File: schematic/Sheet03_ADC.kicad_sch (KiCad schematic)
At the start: 15 parts, among them U1 ADC12DJ5200-SP

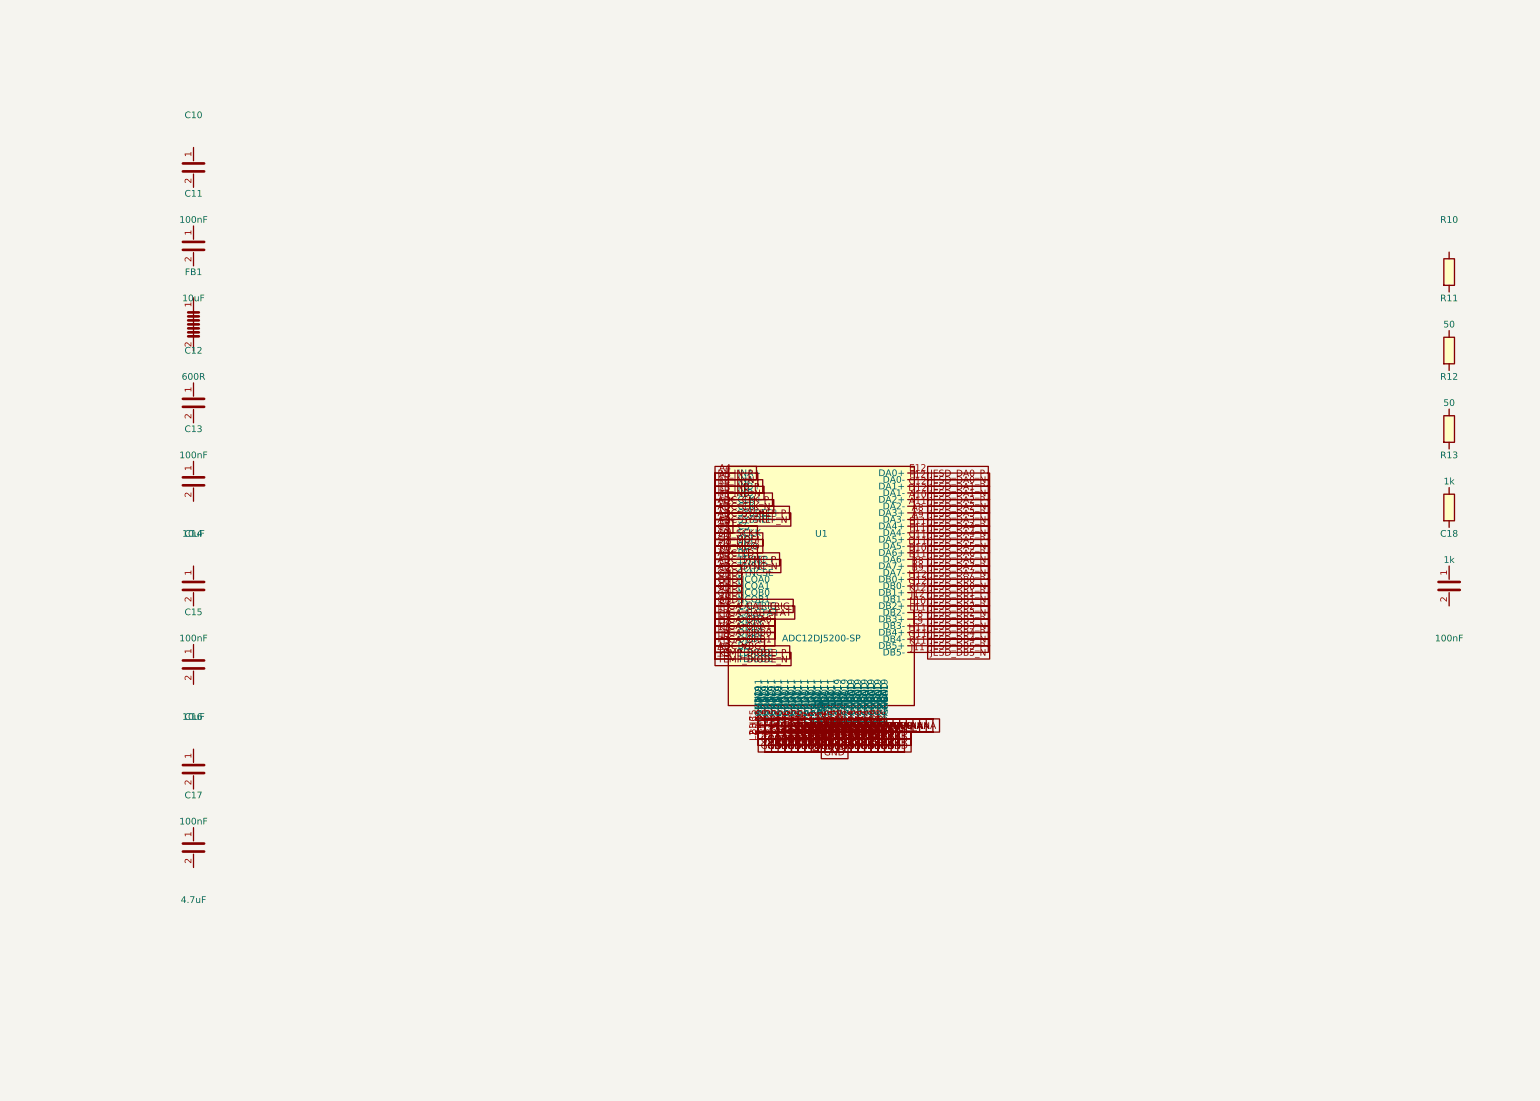
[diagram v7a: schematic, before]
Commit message: feat: connect ALL passive components and fix clock routing
- Added PASSIVE_TOPOLOGY dict mapping 139 passives to their nets
- Passive pin endpoints now get global_labels (was 0 connected, now 138)
- R38 intentionally GND-GND (RECAL_EN pull-down)
- Fixed LMK clock output mapping: CLKout0→ADC_CLK_P, CLKout2→FPGA_REFCLK_P, etc.
- Fixed TPS7H5001-SP SYNC pin collision with LMX_SYNC
- Total connections: 867 pins (up from 641)
- Cross-sheet nets: 52
- Power rails: VIN(33), +3V3(98), GND(228) all with decoupling
- JESD204C: U1↔U2 on 4 lanes ✓
- SPI: U1↔U2↔U3↔U4 ✓
- Clock: LMK→ADC (CLK+SYSREF), LMK→FPGA (REF+SPW) ✓
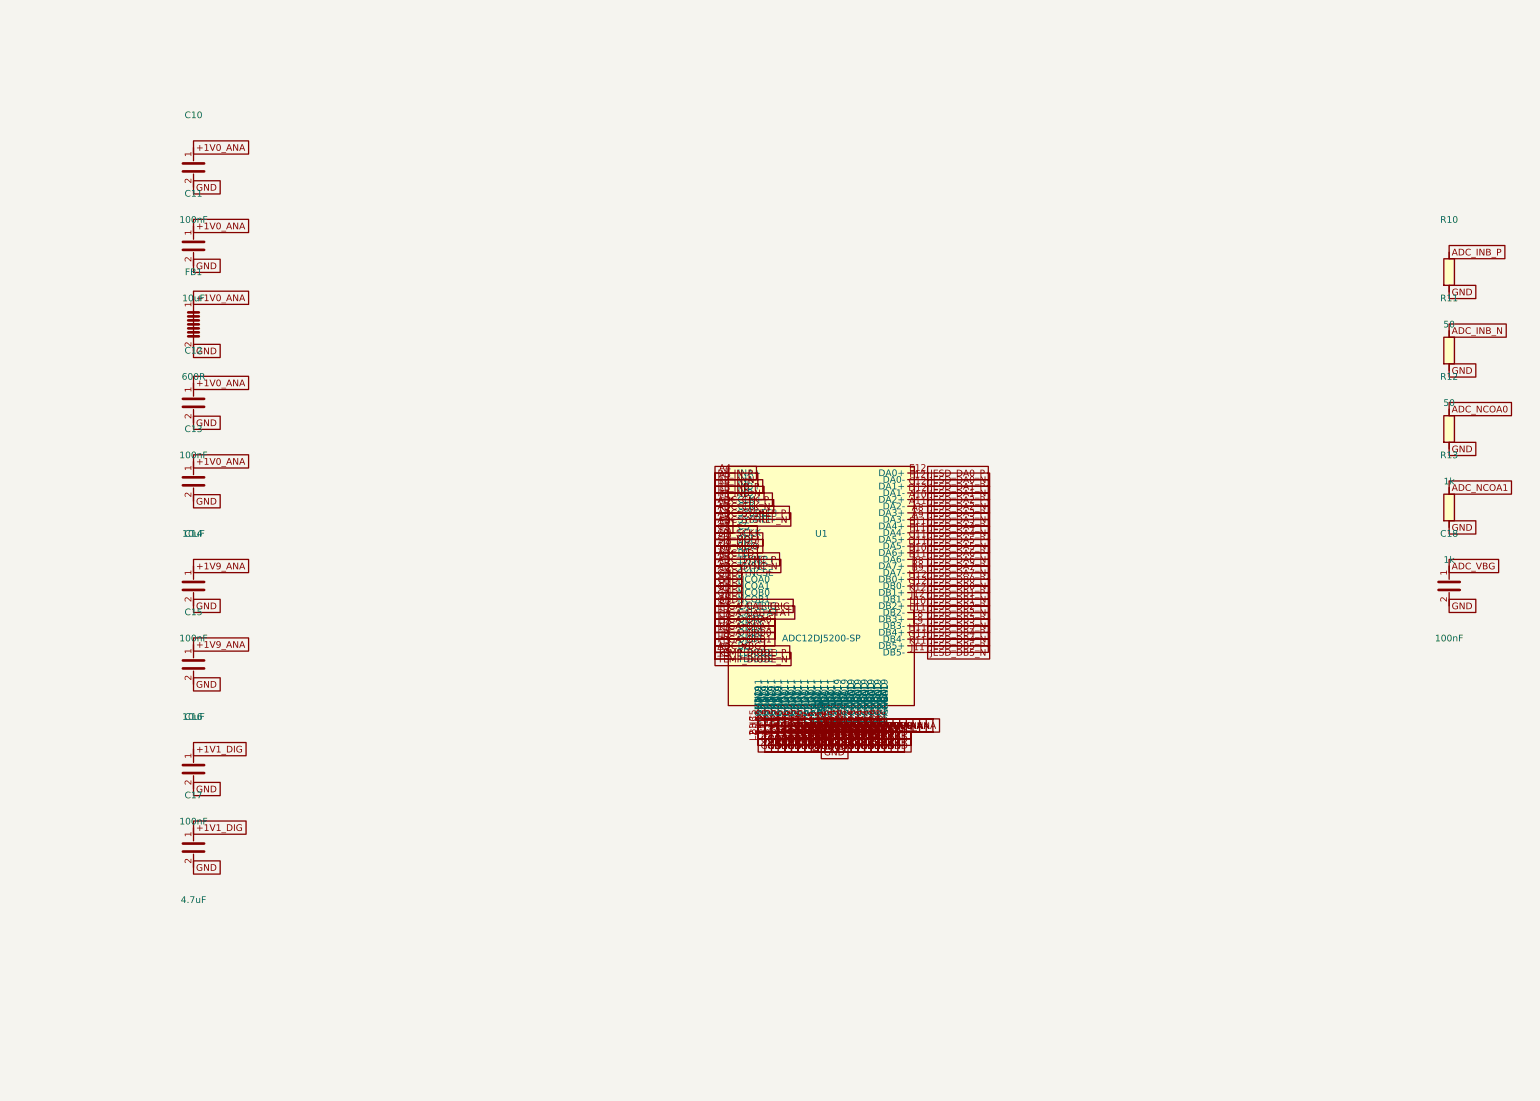
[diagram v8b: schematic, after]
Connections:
- net +1V0_ANA: now also C10.1, C11.1, C12.1, C13.1, FB1.1
- net +1V1_DIG: now also C16.1, C17.1
- net +1V9_ANA: now also C14.1, C15.1
- net ADC_VBG: now also C18.1
- net GND: now also C10.2, C11.2, C12.2, C13.2, C14.2, C15.2, C16.2, C17.2, C18.2, FB1.2, R10.2, R11.2, R12.2, R13.2
- net ADC_INB_N: now reaches R11.1
- net ADC_NCOA0: now reaches R12.1
- net ADC_INB_P: now reaches R10.1
- net ADC_NCOA1: now reaches R13.1
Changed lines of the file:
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@@
   (global_label "GND" (at 212.0650 150.4801 0) (effects (font (size 1.27 1.27))))
   (global_label "GND" (at 200.0000 151.7501 0) (effects (font (size 1.27 1.27))))
+  (global_label "+1V0_ANA" (at 80.0000 36.1900 0) (effects (font (size 1.27 1.27))))
+  (global_label "GND" (at 80.0000 43.8100 0) (effects (font (size 1.27 1.27))))
+  (global_label "+1V0_ANA" (at 80.0000 51.1900 0) (effects (font (size 1.27 1.27))))
+  (global_label "GND" (at 80.0000 58.8100 0) (effects (font (size 1.27 1.27))))
+  (global_label "+1V0_ANA" (at 80.0000 64.9200 0) (effects (font (size 1.27 1.27))))
+  (global_label "GND" (at 80.0000 75.0800 0) (effects (font (size 1.27 1.27))))
+  (global_label "+1V0_ANA" (at 80.0000 81.1900 0) (effects (font (size 1.27 1.27))))
+  (global_label "GND" (at 80.0000 88.8100 0) (effects (font (size 1.27 1.27))))
+  (global_label "+1V0_ANA" (at 80.0000 96.1900 0) (effects (font (size 1.27 1.27))))
+  (global_label "GND" (at 80.0000 103.8100 0) (effects (font (size 1.27 1.27))))
+  (global_label "+1V9_ANA" (at 80.0000 116.1900 0) (effects (font (size 1.27 1.27))))
+  (global_label "GND" (at 80.0000 123.8100 0) (effects (font (size 1.27 1.27))))
+  (global_label "+1V9_ANA" (at 80.0000 131.1900 0) (effects (font (size 1.27 1.27))))
+  (global_label "GND" (at 80.0000 138.8100 0) (effects (font (size 1.27 1.27))))
+  (global_label "+1V1_DIG" (at 80.0000 151.1900 0) (effects (font (size 1.27 1.27))))
+  (global_label "GND" (at 80.0000 158.8100 0) (effects (font (size 1.27 1.27))))
+  (global_label "+1V1_DIG" (at 80.0000 166.1900 0) (effects (font (size 1.27 1.27))))
+  (global_label "GND" (at 80.0000 173.8100 0) (effects (font (size 1.27 1.27))))
+  (global_label "ADC_VBG" (at 320.0000 116.1900 0) (effects (font (size 1.27 1.27))))
+  (global_label "GND" (at 320.0000 123.8100 0) (effects (font (size 1.27 1.27))))
+  (global_label "ADC_INB_P" (at 320.0000 56.1900 0) (effects (font (size 1.27 1.27))))
+  (global_label "GND" (at 320.0000 63.8100 0) (effects (font (size 1.27 1.27))))
+  (global_label "ADC_INB_N" (at 320.0000 71.1900 0) (effects (font (size 1.27 1.27))))
+  (global_label "GND" (at 320.0000 78.8100 0) (effects (font (size 1.27 1.27))))
+  (global_label "ADC_NCOA0" (at 320.0000 86.1900 0) (effects (font (size 1.27 1.27))))
+  (global_label "GND" (at 320.0000 93.8100 0) (effects (font (size 1.27 1.27))))
+  (global_label "ADC_NCOA1" (at 320.0000 101.1900 0) (effects (font (size 1.27 1.27))))
+  (global_label "GND" (at 320.0000 108.8100 0) (effects (font (size 1.27 1.27))))
   (sheet_instances (path "/" (page "1")))
 )
